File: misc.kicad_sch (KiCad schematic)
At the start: 55 parts, among them J10 Molex_KK_1x4_0470531000, J11 Molex_KK_1x4_0470531000, J9 Molex_KK_1x4_0470531000, Q10 MMBT3904LT1G, Q5 BSS138-7-F, Q6 BSS84AKW, Q7 BSS138-7-F, Q8 BSS138-7-F, Q9 MMBT3904LT1G, U24 ADT7476AARQZ, U25 74LVC1G157-Q100H_SOT457, U26 74LVC1G157-Q100H_SOT457, U27 NTS0102_TSSOP, U28 NTS0102_TSSOP, U29 NTS0102_TSSOP

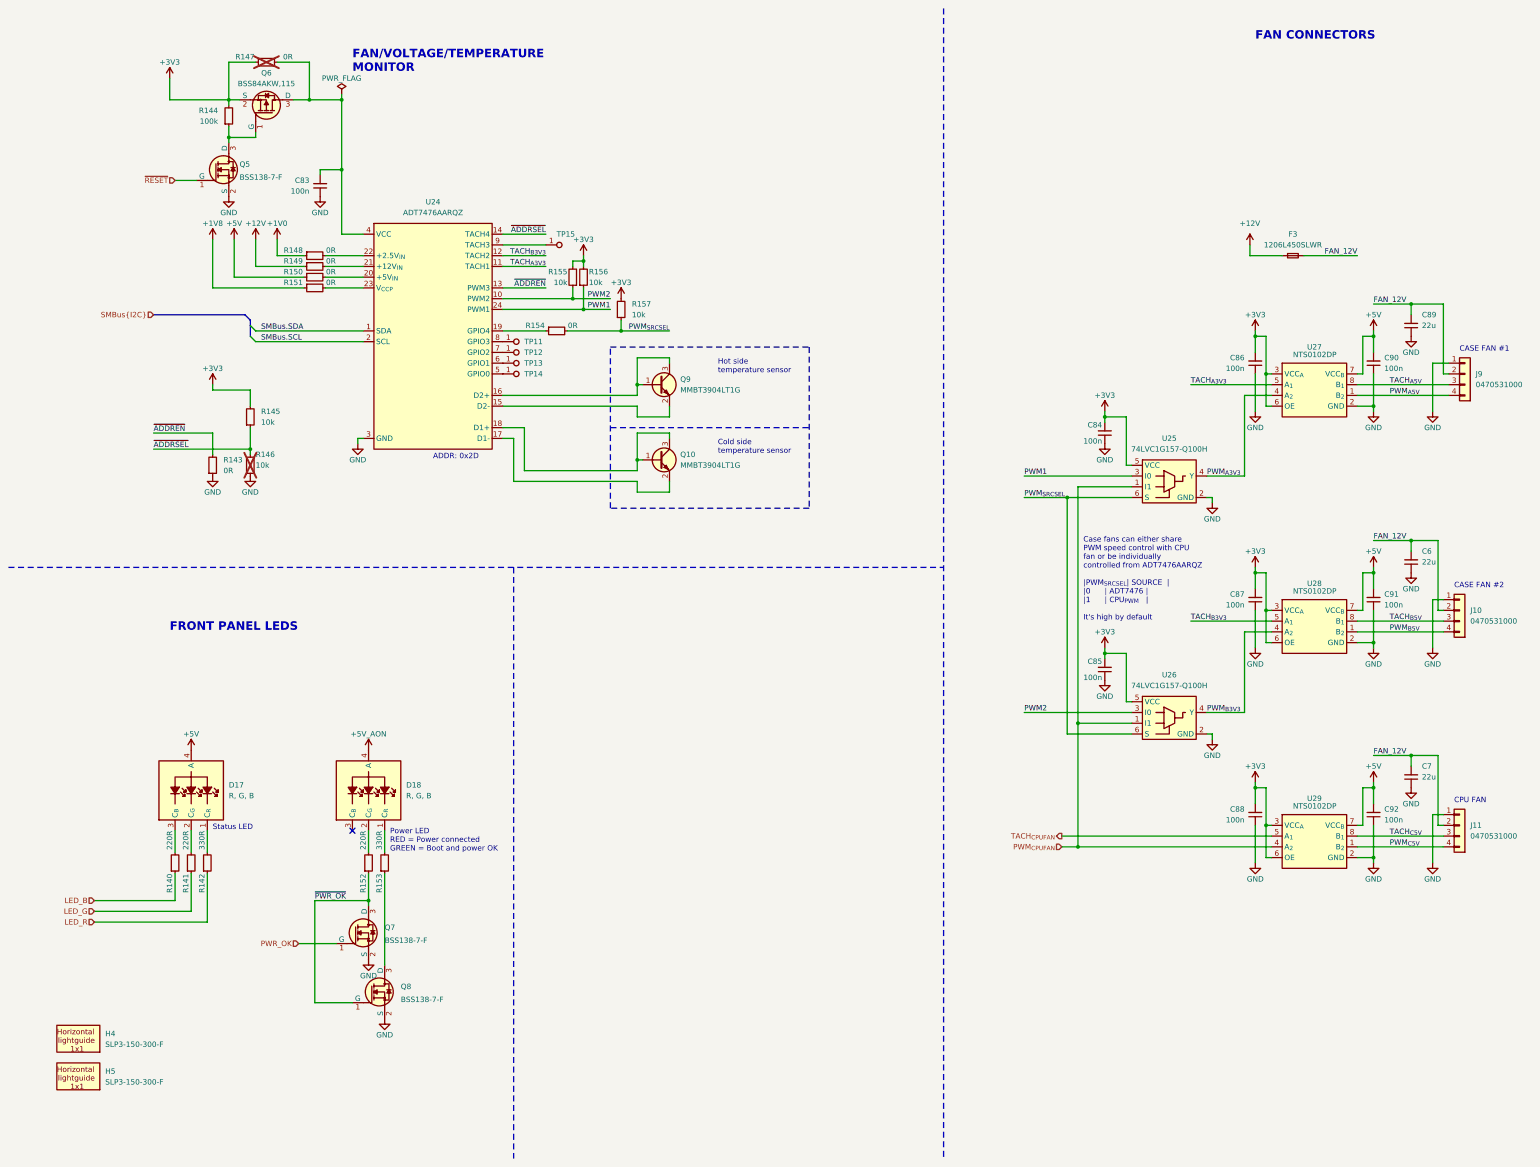
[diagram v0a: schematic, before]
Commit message: [#70030] Unify functional block names
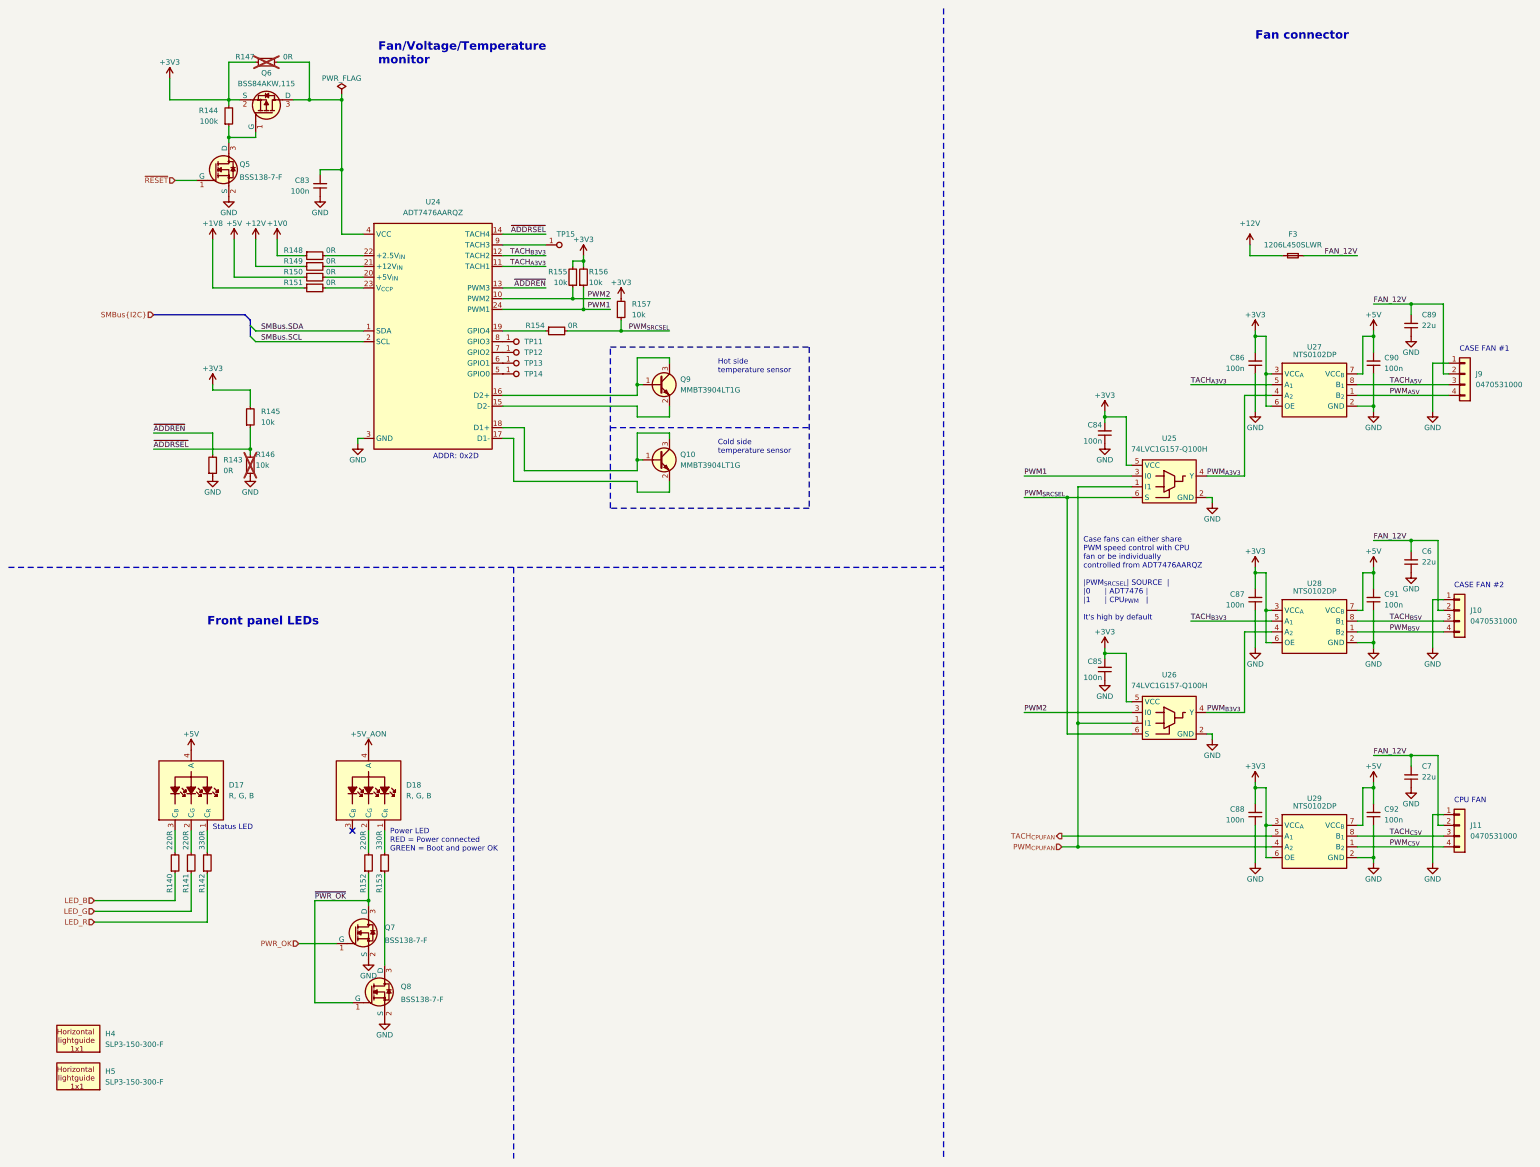
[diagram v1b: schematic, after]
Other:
- note added: "Fan connector"
- note added: "Fan/Voltage/Temperature monitor"
- note added: "Front panel LEDs"
- note removed: "FAN CONNECTORS"
- note removed: "FAN/VOLTAGE/TEMPERATURE MONITOR"
- note removed: "FRONT PANEL LEDS"
- company: Antmicro Ltd. -> Antmicro Ltd
- title: Com Express 7 baseboard -> COM Express 7 Baseboard
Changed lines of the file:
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@@
 	(paper "A3")
 	(title_block
-		(title "Com Express 7 baseboard")
-		(date "2024-03-28")
+		(title "COM Express 7 Baseboard")
+		(date "2024-12-13")
 		(rev "1.1.0")
-		(company "Antmicro Ltd.")
+		(company "Antmicro Ltd")
+		(comment 1 "www.antmicro.com")
 	)
 	(junction
@@
 		)
 	)
-	(text "FRONT PANEL LEDS"
+	(text "Front panel LEDs"
 		(exclude_from_sim no)
-		(at 50.8 160.02 0)
+		(at 59.69 158.75 0)
 		(effects
 			(font
@@
 		)
 	)
-	(text "FAN/VOLTAGE/TEMPERATURE\nMONITOR"
+	(text "Fan/Voltage/Temperature\nmonitor"
 		(exclude_from_sim no)
-		(at 93.98 27.94 0)
+		(at 100.076 26.162 0)
 		(effects
 			(font
@@
 		)
 	)
-	(text "FAN CONNECTORS"
+	(text "Fan connector"
 		(exclude_from_sim no)
 		(at 307.34 20.32 0)

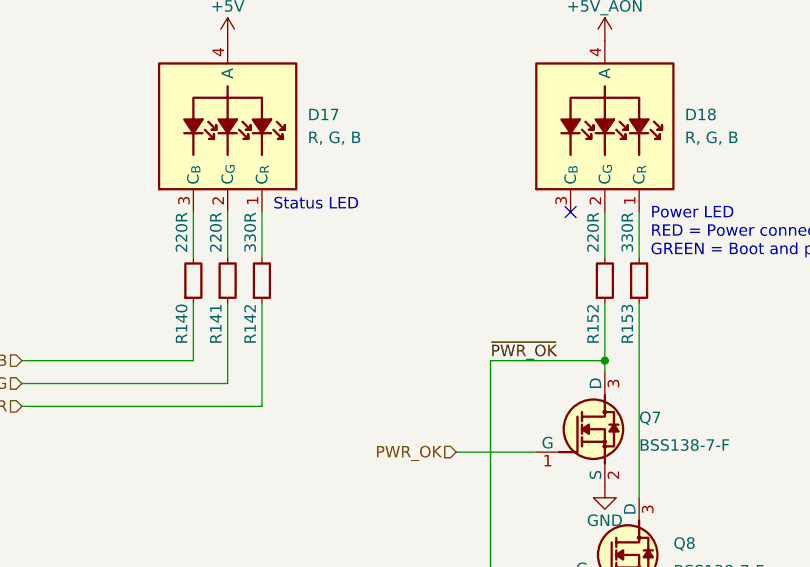
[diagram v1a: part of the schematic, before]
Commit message: [#70532] Increase D17 and D18 LED's resistors to 10k
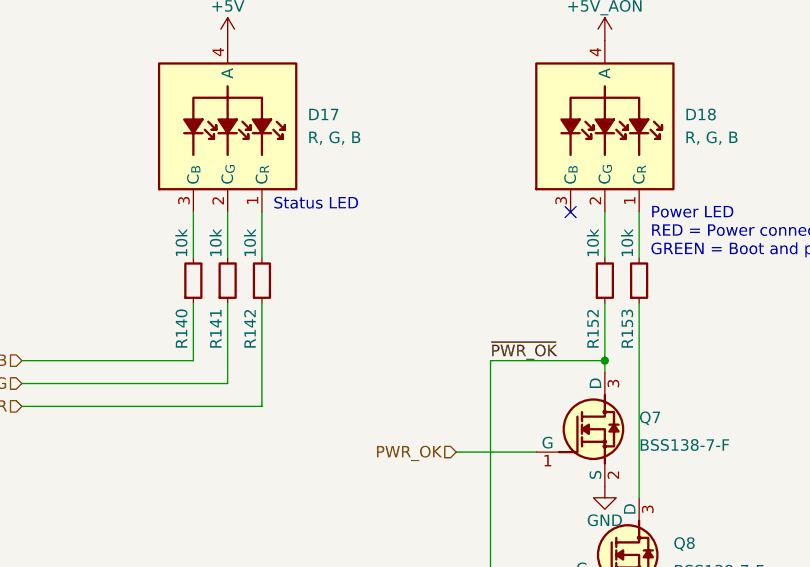
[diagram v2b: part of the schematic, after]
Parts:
- removed R140, R141, R152: R_220R_0402, antmicro-footprints:R_0402_1005Metric, symbol antmicroResistors0402:R_220R_0402
- removed R142, R153: R_330R_0402, antmicro-footprints:R_0402_1005Metric, symbol antmicroResistors0402:R_330R_0402
- added R140, R141, R142, R152, R153: R_10k_0402, antmicro-footprints:R_0402_1005Metric, symbol antmicroResistors0402:R_10k_0402
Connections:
- net LED_B: now also R140.1
- net LED_G: now also R141.1
- net LED_R: now also R142.1
- net ~{PWR_OK}: now also R152.1
- net at D17.2 (C_{G}): now also R141.2
- net at D17.1 (C_{R}): now also R142.2
- net at D17.3 (C_{B}): now also R140.2
- net at Q8.3 (D): now also R153.1
- net at D18.1 (C_{R}): now also R153.2
- net at D18.2 (C_{G}): now also R152.2
